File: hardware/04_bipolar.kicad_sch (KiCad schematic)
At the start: 23 parts, among them U4 TPS65131RGER

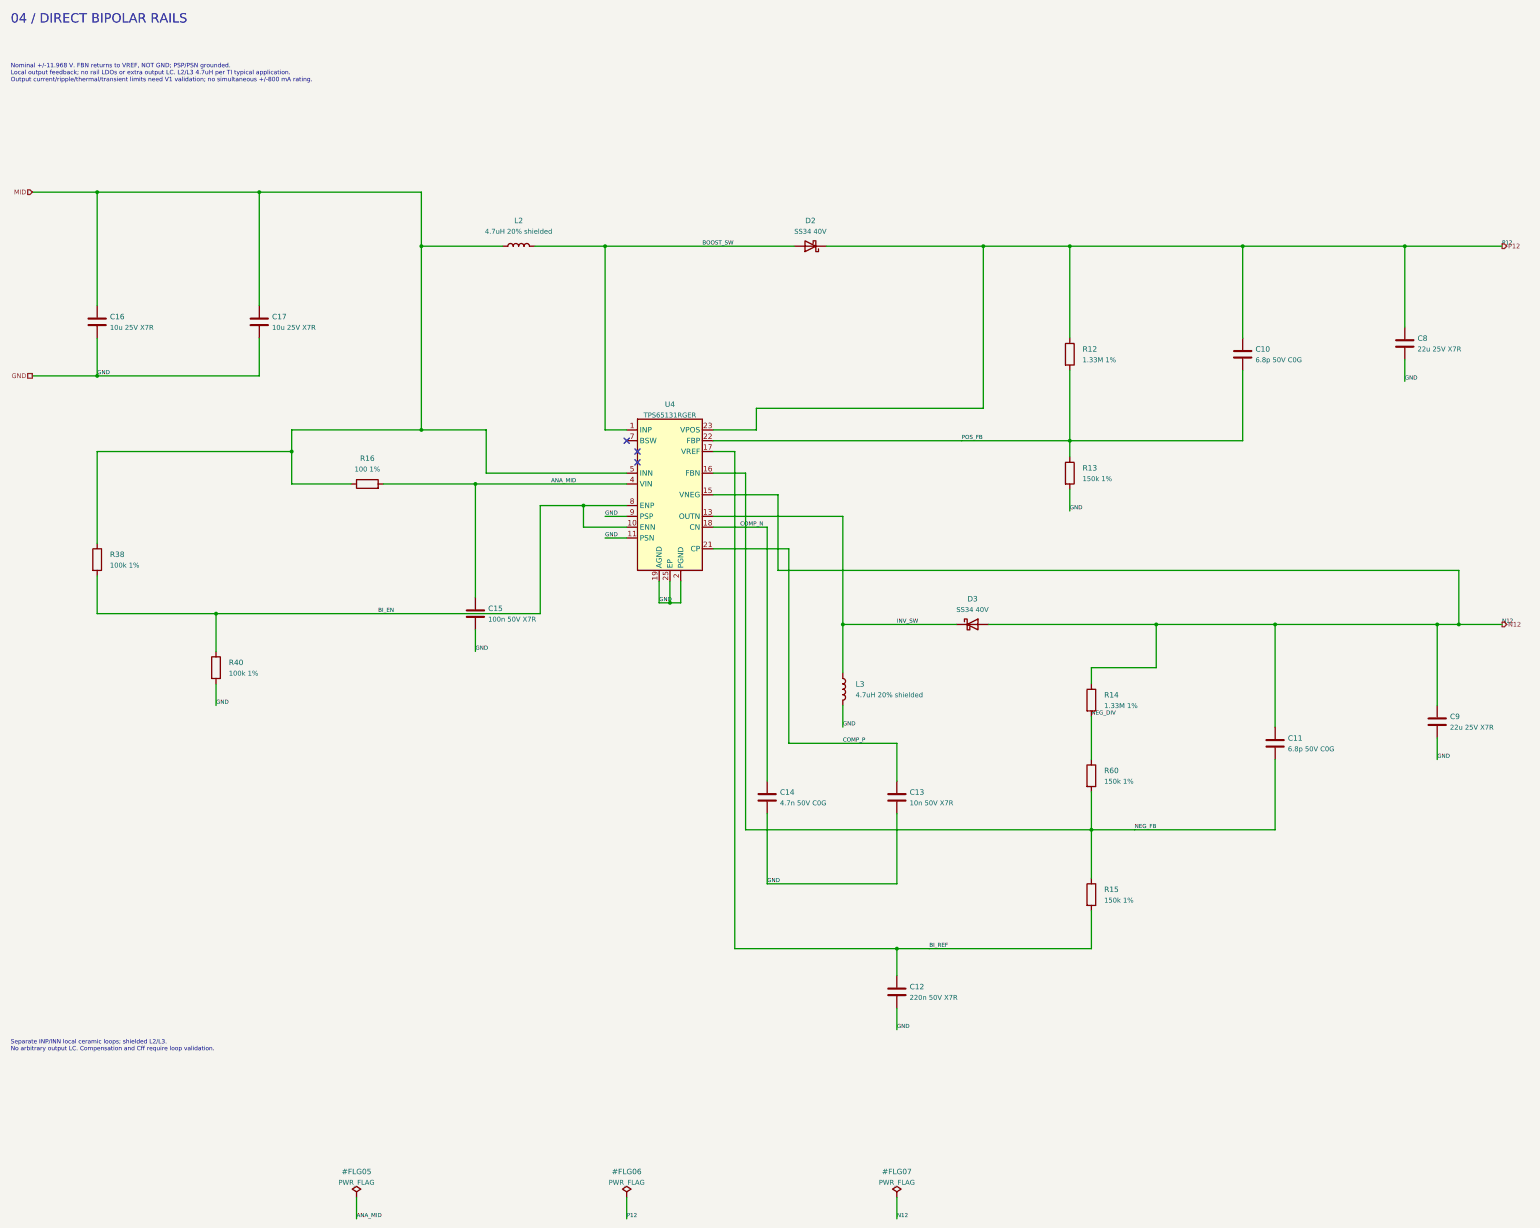
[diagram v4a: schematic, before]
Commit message: Complete four-layer routing, adopt proven HRO USB-C and release checked fabrication files
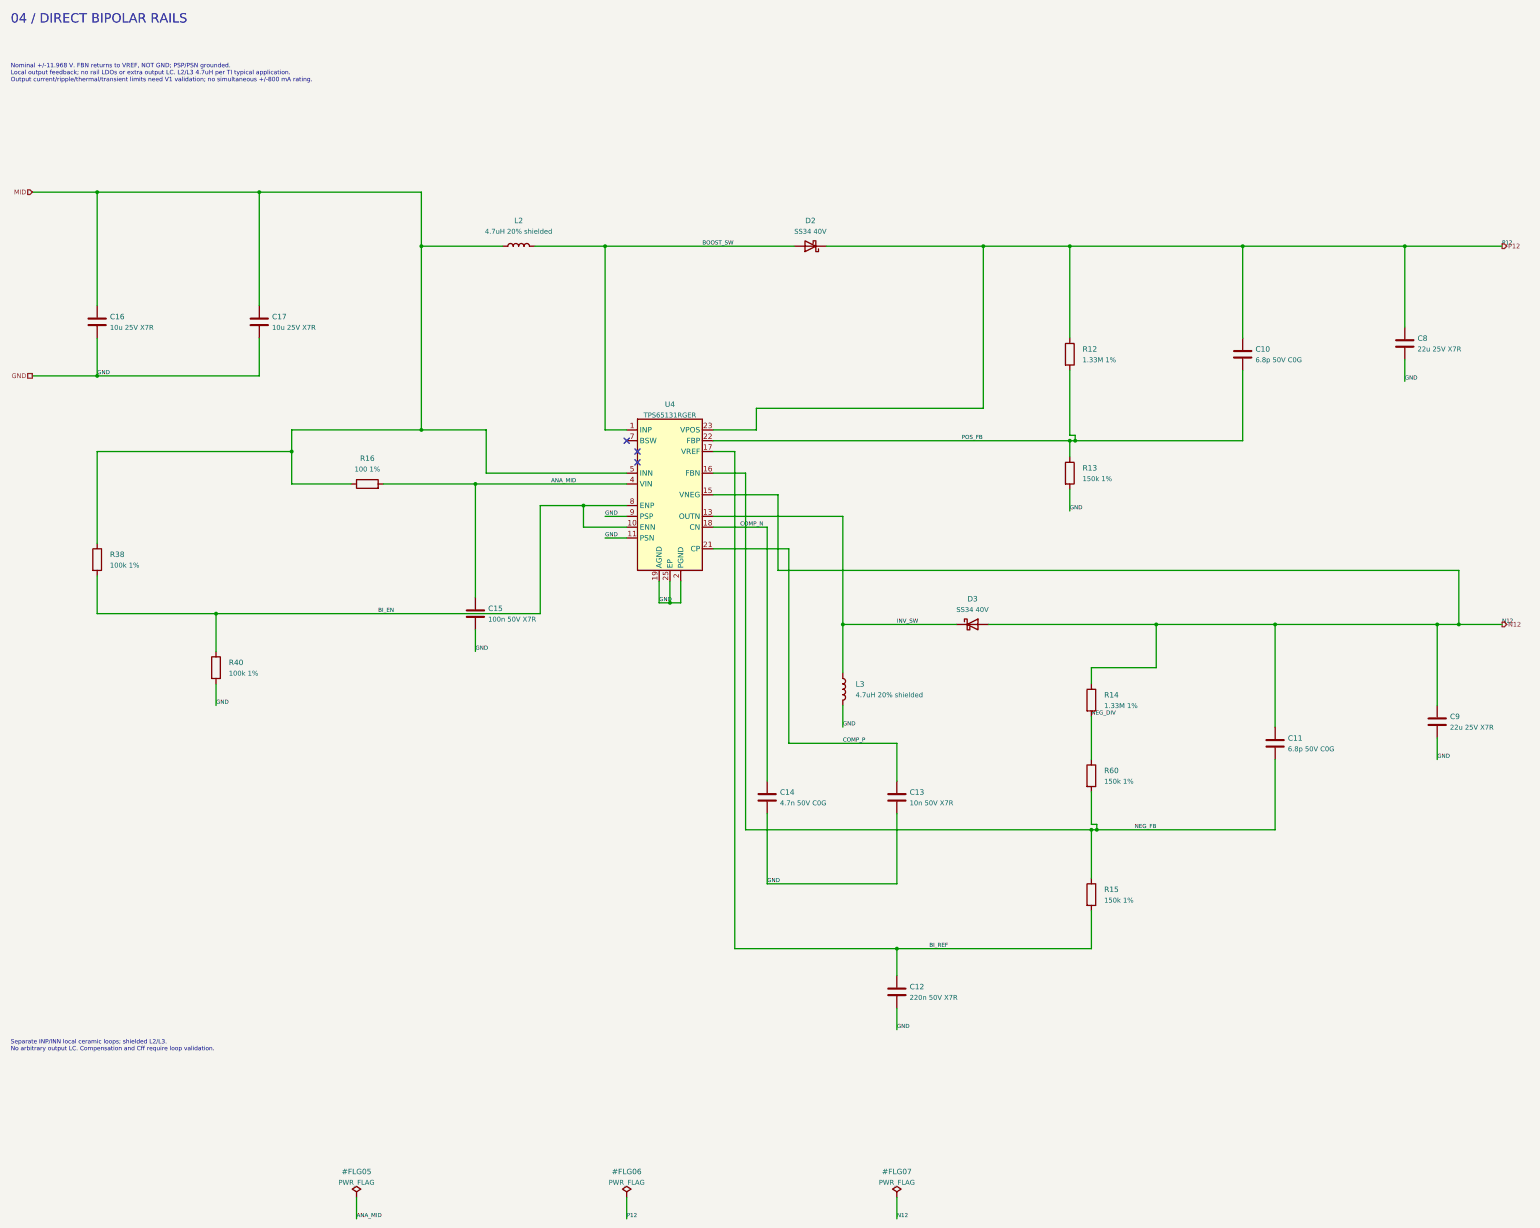
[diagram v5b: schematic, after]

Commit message: Add low-noise ±12 V LDO prototype supply and verified LDO-R1 fabrication release
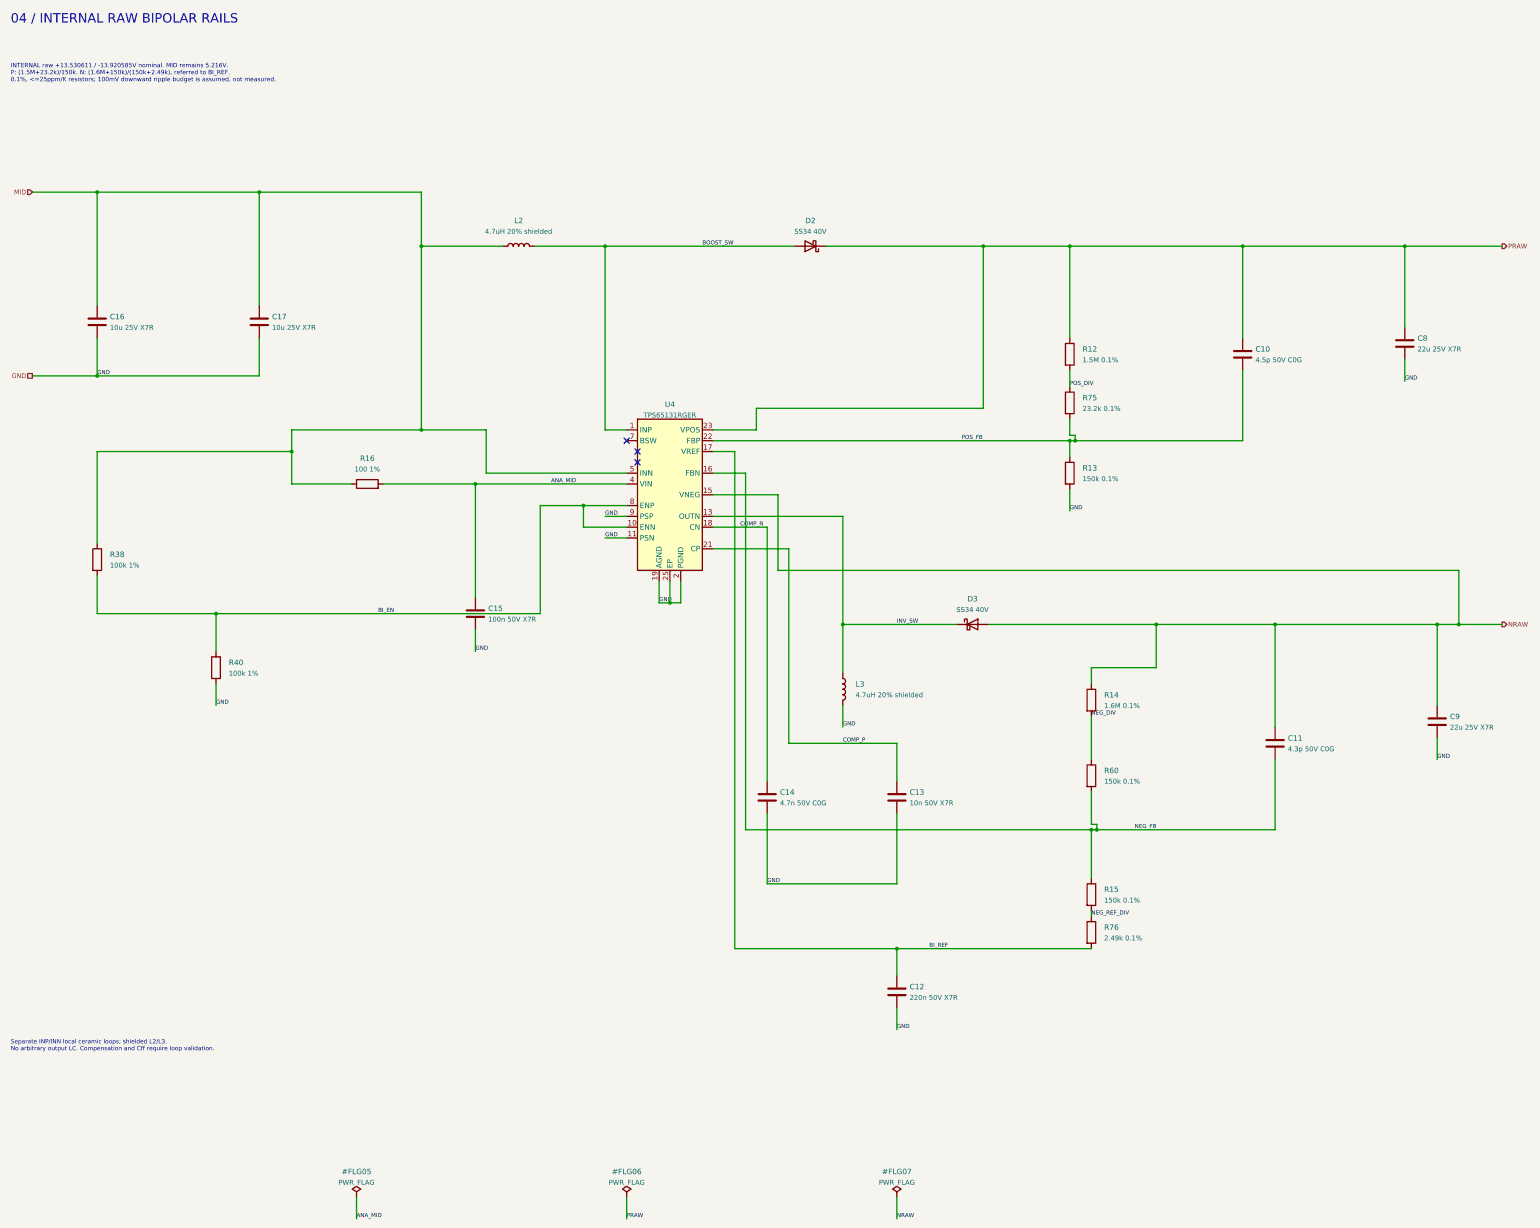
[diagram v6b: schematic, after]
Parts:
- added R75: 23.2k 0.1%, BigModular:R_0603_1608Metric, symbol BigModular:Device_R
- added R76: 2.49k 0.1%, BigModular:R_0603_1608Metric, symbol BigModular:Device_R
- C10: value 6.8p 50V C0G -> 4.5p 50V C0G
- C11: value 6.8p 50V C0G -> 4.3p 50V C0G
- R12: value 1.33M 1% -> 1.5M 0.1%; footprint BigModular:R_0603_1608Metric -> BigModular:R_0805_2012Metric; LCSC C482628 -> (none); MPN RC0603FR-071M33L -> CPF0805B1M5E1; Manufacturer (none) -> TE Connectivity; NOTE Prototype candidate; qualify ratings, land pattern and oper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 -> Approved raw +13.530611/-13.920585V: 0.1%, <=25ppm/K. R12+R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
- R13, R15, R60: value 150k 1% -> 150k 0.1%; LCSC C22807 -> C326734; MPN 0603WAF1503T5E -> RT0603BRD07150KL; Manufacturer (none) -> YAGEO; NOTE Prototype candidate; qualify ratings, land pattern and oper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 -> Approved raw +13.530611/-13.920585V: 0.1%, <=25ppm/K. R12+R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
- R14: value 1.33M 1% -> 1.6M 0.1%; footprint BigModular:R_0603_1608Metric -> BigModular:R_0805_2012Metric; LCSC C482628 -> C2088870; MPN RC0603FR-071M33L -> CPF0805B1M6E1; Manufacturer (none) -> TE Connectivity; NOTE Prototype candidate; qualify ratings, land pattern and oper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 -> Approved raw +13.530611/-13.920585V: 0.1%, <=25ppm/K. R12+R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
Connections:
- net BI_REF: now also R76.2; no longer R15.2
- net POS_FB: now also R75.2; no longer R12.2
- net N12 renamed NRAW
- net P12 renamed PRAW
- new net NEG_REF_DIV: R15.2, R76.1
- new net POS_DIV: R12.2, R75.1
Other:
- note added: "04 / INTERNAL RAW BIPOLAR RAILS"
- note added: "INTERNAL raw +13.530611 / -13.920585V nominal. MID remains 5.216V. P: (1.5M+23.2k)/150k. N: (1.6M+150k)/(150k+2.49k), referred to BI_REF. 0.1%, <=25ppm/K resistors; 100mV downward ripple budget is assumed, not measured."
- note removed: "04 / DIRECT BIPOLAR RAILS"
- note removed: "Nominal +/-11.968 V. FBN returns to VREF, NOT GND; PSP/PSN grounded. Local output feedback; no rail LDOs or extra output LC. L2/L3 4.7uH per TI typical application. Output current/ripple/thermal/transient limits need V1 validation; no simultaneous +/-800 mA rating."

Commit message: Use standard vias and front-only Economy assembly with Basic passive networks and DNP LED
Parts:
- C10: footprint BigModular:C_0603_1608Metric -> BigModular:C_0402_1005Metric; LCSC (none) -> C501829; MPN (none) -> 0402CG4R5C500NT; Manufacturer (none) -> FH (Guangdong Fenghua Advanced Tech); NOTE Effective capacitance under DC bias and temperature must be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 -> FH 0402CG4R5C500NT, 4.5pF +/-0.25pF, 50V C0G; authorized 04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
- C11: LCSC (none) -> C519375; MPN (none) -> CC0603CRNPO9BN4R3; Manufacturer (none) -> YAGEO; NOTE Effective capacitance under DC bias and temperature must be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 -> YAGEO CC0603CRNPO9BN4R3: 4.3pF +/-0.25pF, 50V NP0; negative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
- C12: LCSC (none) -> C107083; MPN (none) -> CC0603KRX7R9BB224; Manufacturer (none) -> YAGEO
- C13: LCSC (none) -> C57112; MPN (none) -> 0603B103K500NT; Manufacturer (none) -> FH (Guangdong Fenghua Advanced Tech)
- C14: LCSC (none) -> C576818; MPN (none) -> CC0603JRNPO9BN472; Manufacturer (none) -> YAGEO; NOTE Effective capacitance under DC bias and temperature must be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 -> YAGEO CC0603JRNPO9BN472: 4.7nF +/-5%, 50V NP0. TI recommend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
- C16, C17: LCSC (none) -> C14860; MPN (none) -> CL31B106KAHNNNE; Manufacturer (none) -> Samsung Electro-Mechanics
- R12: LCSC (none) -> C4223894
- R16: LCSC (none) -> C22775; MPN (none) -> 0603WAF1000T5E; Manufacturer (none) -> UNI-ROYAL(Uniroyal Elec)
- R75: LCSC (none) -> C861244
- R76: LCSC (none) -> C861299
